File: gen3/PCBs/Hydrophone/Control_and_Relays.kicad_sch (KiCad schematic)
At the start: 9 parts, among them U1 MCP23017x-x-SS, U2 MCP23017x-x-SS, U3 MCP23017x-x-SS

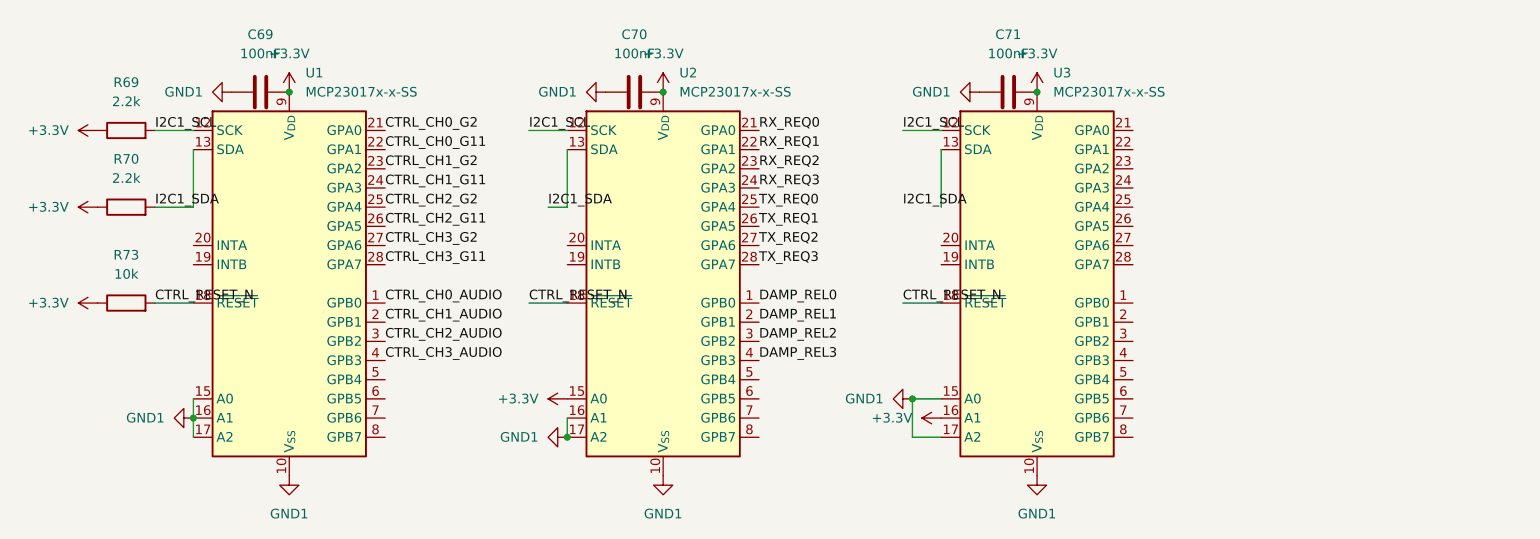
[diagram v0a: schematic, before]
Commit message: fix small bugs in IO expander sheet
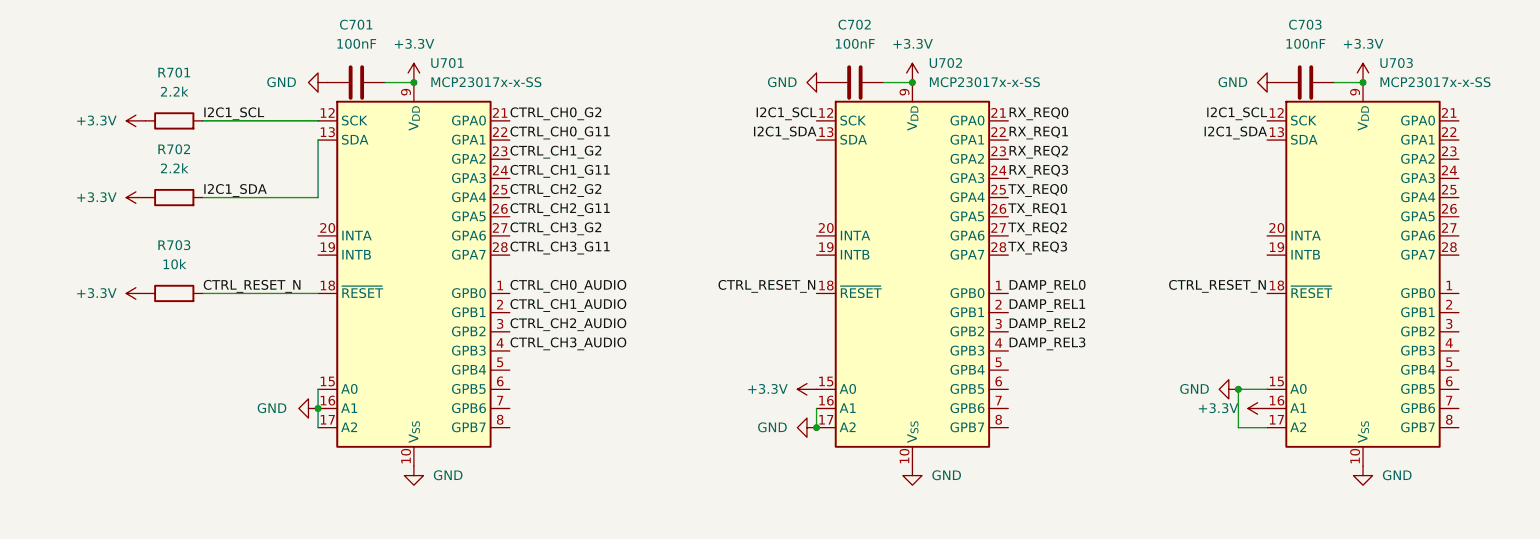
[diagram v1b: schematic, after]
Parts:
- renumbered C69 to C701, C70 to C702, C71 to C703, R69 to R701, R70 to R702, R73 to R703, U1 to U701, U2 to U702, U3 to U703
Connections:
- net I2C1_SDA: now also U703.13 (SDA)
- net GND1 renamed GND
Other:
- moved on the sheet: C701, C702, C703, R701, R702, R703, U701, U702, U703
